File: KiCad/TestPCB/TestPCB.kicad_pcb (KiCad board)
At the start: 2 copper layers, 71 parts, among them Q2 Q_Photo_NPN, Q5 2N7000, Q6 2N7000, U1 ESP32-S3-WROOM-1, U2 TC1185-xCT, U3 MCP73831-2-OT, U4 LSM6DSM

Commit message: ADD: PCB connections finished
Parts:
- removed Q5, Q6: 2N7000, Package_TO_SOT_THT:TO-92_Inline
- added C3: 4.7µF, Capacitor_SMD:C_0805_2012Metric, F.Cu at (104.1, 84.2)
- added C4: 4.7µF, Capacitor_SMD:C_0805_2012Metric, F.Cu at (123.2, 84.2)
- added C5: 1µF, Capacitor_SMD:C_0805_2012Metric, F.Cu at (127.0, 83.8)
- added C6: 470pF, Capacitor_SMD:C_0805_2012Metric, F.Cu at (133.3, 92.7)
- added C7: 1µF, Capacitor_SMD:C_0805_2012Metric, F.Cu at (138.4, 92.7)
- added D1: LED, LED_SMD:LED_0805_2012Metric, F.Cu at (114.3, 89.3)
- added J2: USB4135-GF-A, USB4135-GF-A:USB4135GFA, F.Cu at (96.5, 85.5)
- added Q1: SFH_3711, SFH_3711:SFH3711, F.Cu at (102.9, 58.4)
- added Q3: 2N7002, 2N7002:SOT96P240X120-3N, F.Cu at (181.2, 74.9)
- added R5: 2kΩ, Resistor_SMD:R_0805_2012Metric, F.Cu at (113.0, 85.5)
- added R6: 330Ω, Resistor_SMD:R_0805_2012Metric, F.Cu at (113.0, 81.7)
- added S1: KMR631NGULCLFS, KMR631NGULCLFS:KMR621NG, F.Cu at (101.9, 65.2)
- added S2: JS202011SCQN, JS202011SCQN:JS202011SCQN, F.Cu at (134.7, 73.9)
- Q2: value Q_Photo_NPN -> 2N7002; footprint LED_SMD:LED_0805_2012Metric -> 2N7002:SOT96P240X120-3N
- moved TP12 96.6 mm to (193.5, 79.5)
- moved TP14 90.6 mm to (193.5, 84.6)
- moved TP16 84.8 mm to (185.9, 87.2)
- moved TP8 84.3 mm to (180.8, 87.2)
- moved TP15 83.2 mm to (174.5, 87.2)
- moved TP13 80.2 mm to (185.9, 77.0)
- moved TP11 76.1 mm to (169.4, 87.2)
- moved Q2 72.6 mm to (181.2, 79.5)
- moved TP9 71.9 mm to (168.1, 74.5)
- moved C10 70.3 mm to (188.4, 74.5), turned to -90 degrees
- moved C11 68.4 mm to (188.4, 80.8), turned to 90 degrees
- moved TP10 68.0 mm to (170.7, 79.5)
- moved R11 61.2 mm to (198.6, 74.5)
- moved R12 58.8 mm to (198.6, 84.6)
- moved TP24 57.8 mm to (154.9, 58.4)
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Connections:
- C11 pad 1: Net-(Q6-D) -> Net-(Q2-D)
- Q2 pad 1: Net-(Q2-C) -> Net-(Q2-G)
- Q2 pad 2: Net-(D10-VSS) -> Net-(Q2-S)
- R10 pad 2: Net-(Q6-G) -> Net-(Q2-G)
- R12 pad 1: Net-(Q6-D) -> Net-(Q2-D)
- R9 pad 1: Net-(Q6-S) -> Net-(Q2-S)
- R_Photo2 pad 1: Net-(Q2-C) -> Net-(D10-VSS)
- R_Photo2 pad 2: Net-(R_Photo2-Pad2) -> Net-(Q1-E)
- TP14 pad 1: Net-(Q6-D) -> Net-(Q2-D)
- TP21 pad 1: Net-(J1-SHIELD) -> Net-(U2-GND)
- TP31 pad 1: Net-(R_Photo2-Pad2) -> Net-(Q1-C)
- TP9 pad 1: Net-(Q6-S) -> Net-(Q2-S)
- U2 pad 2: Net-(J1-SHIELD) -> Net-(U2-GND)
- U3 pad 2: Net-(J1-SHIELD) -> Net-(U2-GND)
- U3 pad 4: Net-(J1-SHIELD) -> Net-(U3-V_{DD})
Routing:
- net Net-(U2-GND): track 0.00 -> 82.1 mm
- net Net-(U4-VDD): track 0.00 -> 28.7 mm
- net Net-(Q2-S): track 0.00 -> 26.9 mm
- net Net-(U3-V_{DD}): track 0.00 -> 26.0 mm
- net Net-(U2-VIN): track 0.00 -> 21.5 mm
- net Net-(S2-Pad2): track 0.00 -> 20.5 mm
- net Net-(U4-SCX): track 0.00 -> 20.4 mm
- net Net-(U2-VOUT): track 0.00 -> 19.3 mm
- net Net-(Q2-D): track 0.00 -> 17.7 mm
- net Net-(Q3-D): track 0.00 -> 16.6 mm
- net Net-(Q1-C): track 0.00 -> 13.4 mm
- net Net-(C10-Pad2): track 0.00 -> 12.3 mm
- net Net-(R_Photo2-Pad2): track 12.3 -> 0.00 mm
- net Net-(Q3-S): track 0.00 -> 12.2 mm
- net Net-(D1-A): track 0.00 -> 12.1 mm
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
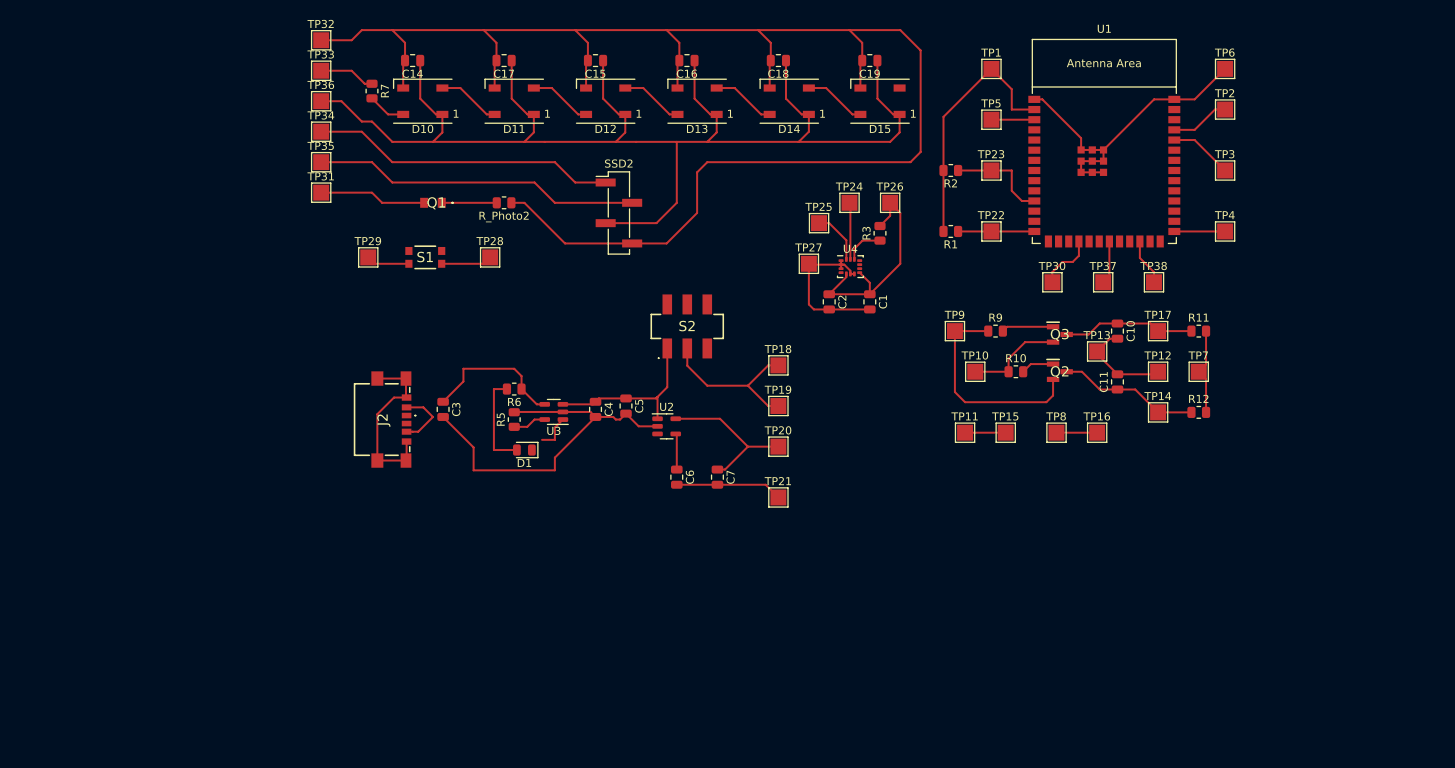
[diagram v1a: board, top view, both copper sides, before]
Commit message: ADD: parts arranged in two pcbs
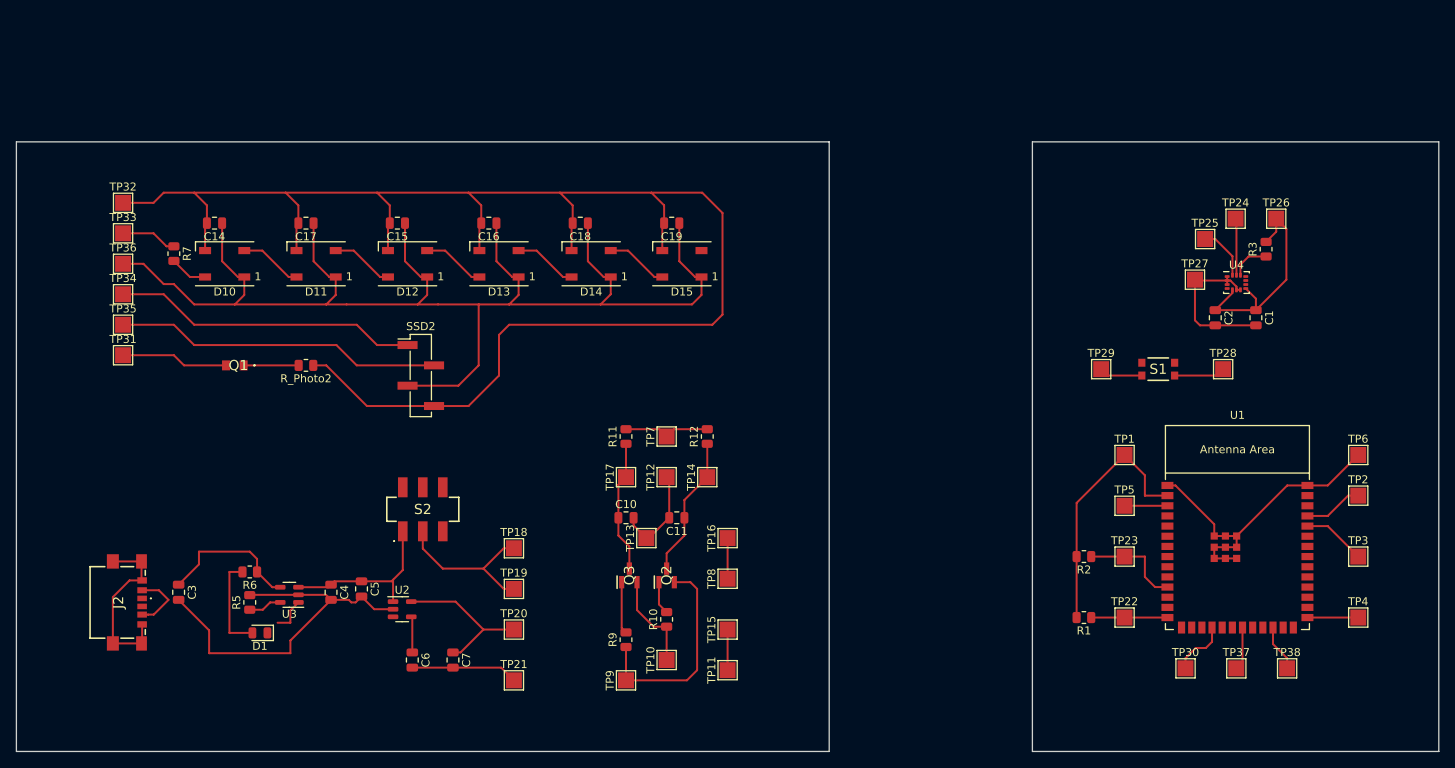
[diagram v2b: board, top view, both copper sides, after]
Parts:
- moved S1 92.7 mm to (193.5, 79.2)
- moved TP29 92.7 mm to (186.4, 79.2)
- moved TP28 92.7 mm to (201.6, 79.2)
- moved R11 72.8 mm to (127.0, 87.6), turned to 90 degrees
- moved TP17 69.0 mm to (127.0, 92.7), turned to 90 degrees
- moved TP7 67.0 mm to (132.1, 87.6), turned to 90 degrees
- moved C10 65.7 mm to (127.0, 97.8), turned to 0 degrees
- moved TP12 62.8 mm to (132.1, 92.7), turned to 90 degrees
- moved Q3 61.7 mm to (127.4, 105.0), turned to 90 degrees
- moved R12 61.5 mm to (137.2, 87.6), turned to 90 degrees
- moved TP13 61.0 mm to (129.5, 100.3), turned to 90 degrees
- moved R9 60.2 mm to (127.0, 113.0), turned to 90 degrees
- moved TP9 60.0 mm to (127.0, 118.1), turned to 90 degrees
- moved C11 57.6 mm to (133.3, 97.8), turned to 180 degrees
- moved TP14 56.9 mm to (137.2, 92.7), turned to 90 degrees
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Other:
- board outline added: 177.8 x 76.2 mm
